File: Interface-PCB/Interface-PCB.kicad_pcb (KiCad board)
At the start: 2 copper layers, 100 x 100 mm, 0 parts

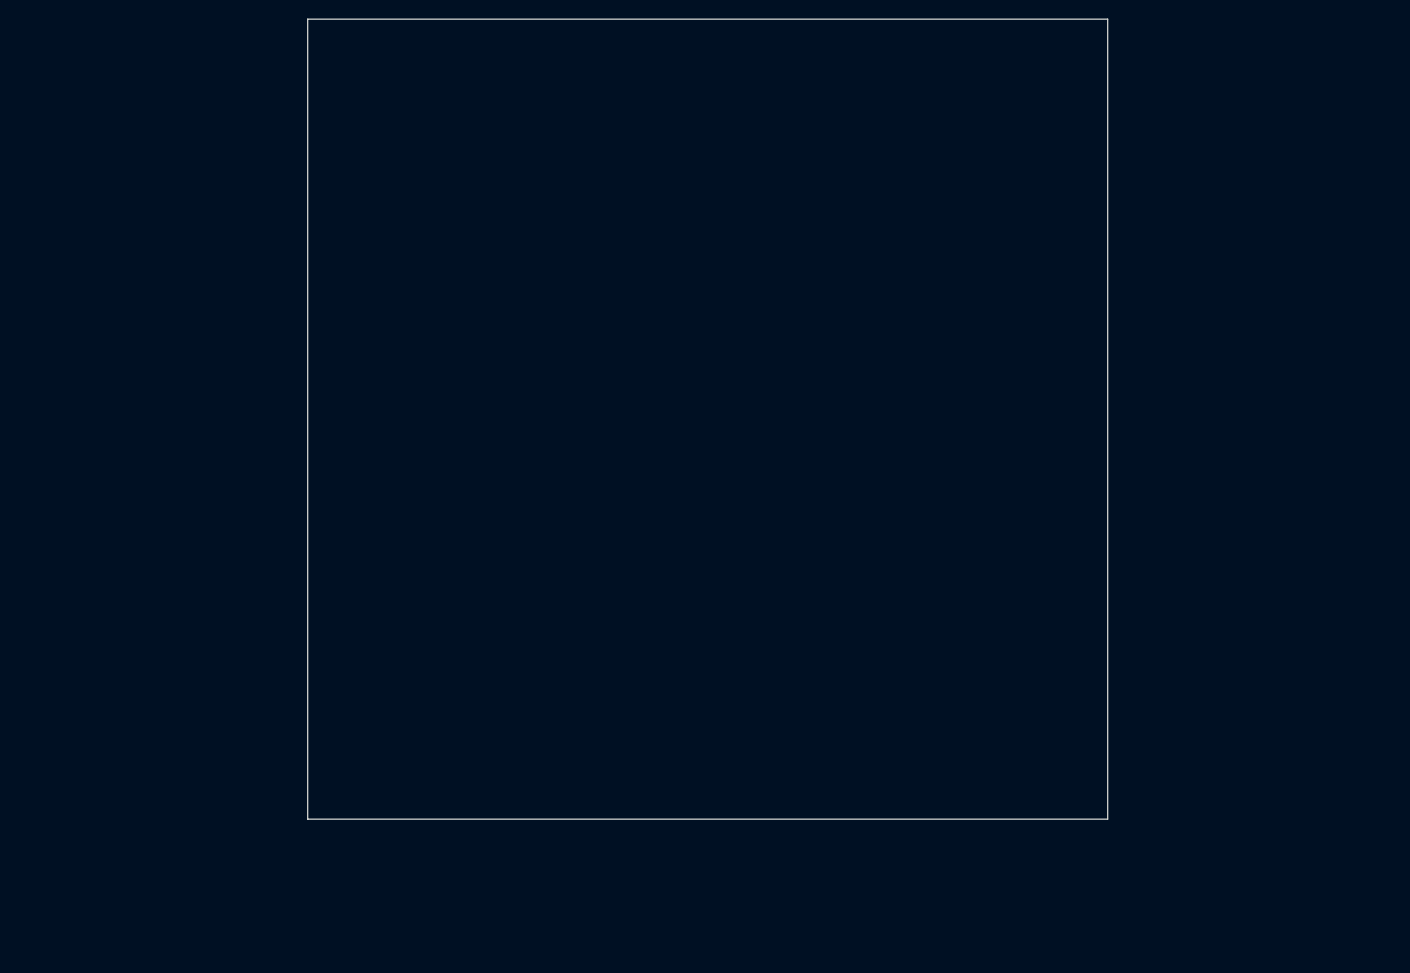
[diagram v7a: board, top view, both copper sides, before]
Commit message: Complete Initial Layout of PCB
- aligned to 5mm grid
- 100x100mm board
- update footprints
- align 2 resistors to 2.54mm spacing
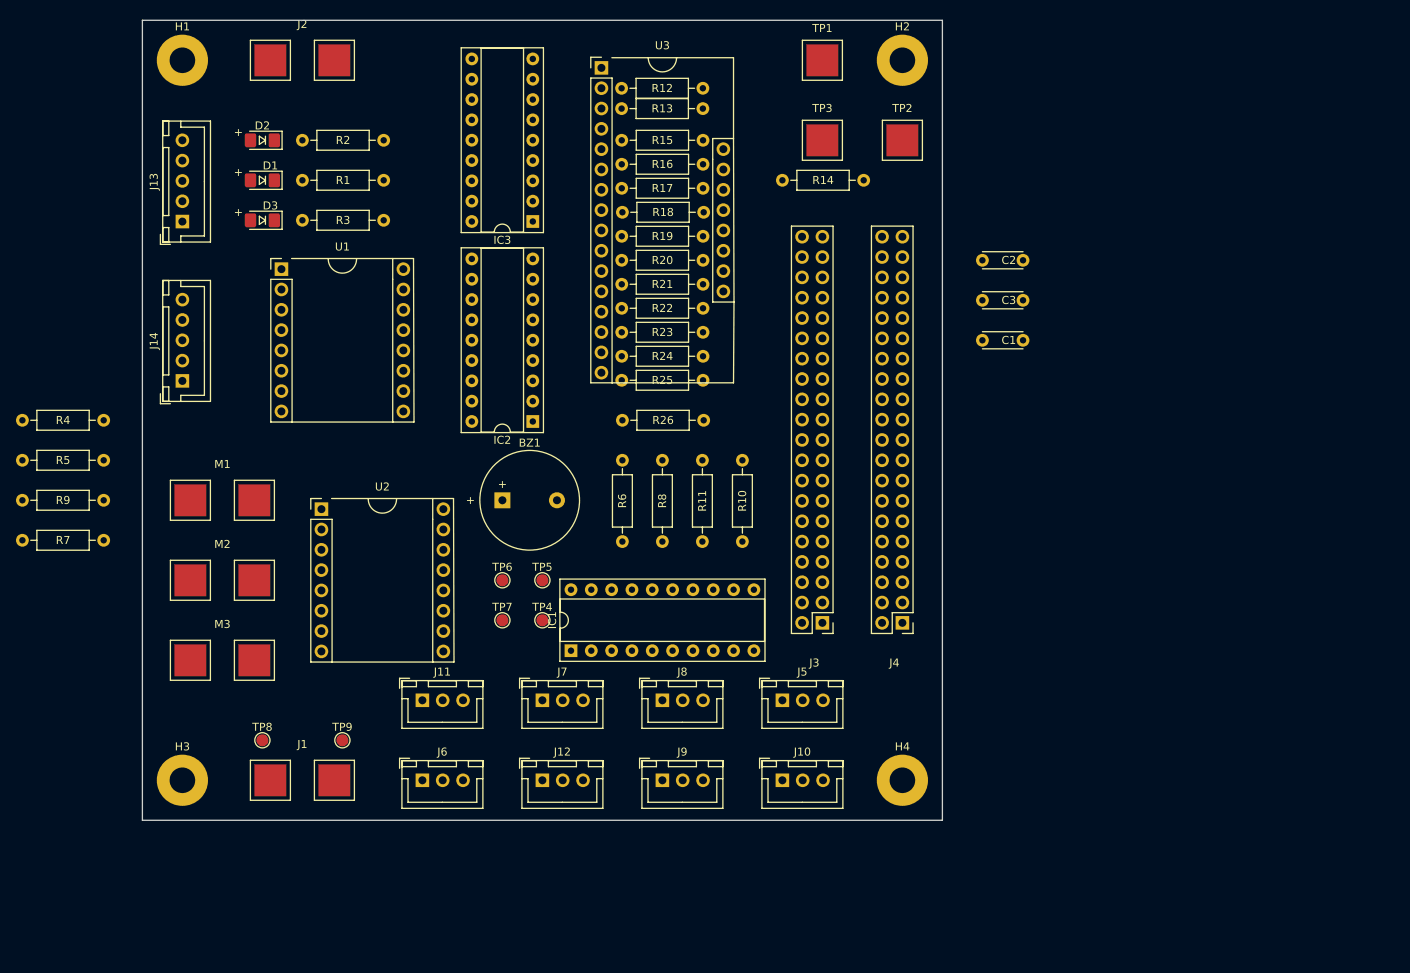
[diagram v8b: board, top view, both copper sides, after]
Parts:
- added BZ1: Buzzer, AA_Custom_Components:Buzzer_Generic_D12.2mm_H6.5mm, F.Cu at (125.0, 110.0)
- added C1: 100nF, AA_Custom_Components:C_Ceramic_Disc_D4.3mm_W1.9mm_P5.08mm, F.Cu at (185.0, 90.0)
- added C2: 100nF, AA_Custom_Components:C_Ceramic_Disc_D4.3mm_W1.9mm_P5.08mm, F.Cu at (185.0, 80.0)
- added C3: 100nF, AA_Custom_Components:C_Ceramic_Disc_D4.3mm_W1.9mm_P5.08mm, F.Cu at (185.0, 85.0)
- added D1: 12V_ON, AA_Custom_Components:LED_SS_1206_3216Metric_Pad1.42x1.75mm_HandSolder, F.Cu at (95.0, 70.0)
- added D2: USER_LED, AA_Custom_Components:LED_SS_1206_3216Metric_Pad1.42x1.75mm_HandSolder, F.Cu at (95.0, 65.0)
- added D3: 5V_ON, AA_Custom_Components:LED_SS_1206_3216Metric_Pad1.42x1.75mm_HandSolder, F.Cu at (95.0, 75.0)
- added H1: MountingHole, MountingHole:MountingHole_3.2mm_M3_Pad, F.Cu at (85.0, 55.0)
- added H2: MountingHole, MountingHole:MountingHole_3.2mm_M3_Pad, F.Cu at (175.0, 55.0)
- added H3: MountingHole, MountingHole:MountingHole_3.2mm_M3_Pad, F.Cu at (85.0, 145.0)
- added H4: MountingHole, MountingHole:MountingHole_3.2mm_M3_Pad, F.Cu at (175.0, 145.0)
- added IC1: SN74LVC245AN, AA_Custom_Components:DIP-20_W7.62mm_Socket_IC, F.Cu at (133.6, 128.8)
- added IC2: TBD62783APG, AA_Custom_Components:DIP-18_W7.62mm_Socket_IC, F.Cu at (128.8, 100.2)
- added IC3: TBD62783APG, AA_Custom_Components:DIP-18_W7.62mm_Socket_IC, F.Cu at (128.8, 75.2)
- added J1: BARREL_JACK_PAD, AA_Custom_Components:PowerPad_Pair_4.0x4.0mm, F.Cu at (100.0, 145.0)
- added J10: LEVEL_SENSOR, AA_Custom_Components:JST_XH_1x03_P2.54mm_Vertical, F.Cu at (160.0, 145.0)
- added J11: TEMPERATURE_SENSOR, AA_Custom_Components:JST_XH_1x03_P2.54mm_Vertical, F.Cu at (115.0, 135.0)
- added J12: TEMPERATURE_SENSOR, AA_Custom_Components:JST_XH_1x03_P2.54mm_Vertical, F.Cu at (130.0, 145.0)
- added J13: CONN_05JST, AA_Custom_Components:JST_XH_1x05_P2.54mm_Vertical, F.Cu at (85.0, 75.2)
- added J14: CONN_05JST, AA_Custom_Components:JST_XH_1x05_P2.54mm_Vertical, F.Cu at (85.0, 95.1)
- added J2: BARREL_JACK_PAD, AA_Custom_Components:PowerPad_Pair_4.0x4.0mm, F.Cu at (100.0, 55.0)
- added J3: GPIO_DEBUG_HEADER, AA_Custom_Components:RASPBERRYPI-40-PIN-GPIO-2x20_P2.54mm_Vertical, F.Cu at (165.0, 125.3)
- added J4: RASPBERRYPI_GPIO_CONN_HEADER, AA_Custom_Components:RASPBERRYPI-40-PIN-GPIO-2x20_P2.54mm_Vertical, F.Cu at (175.0, 125.3)
- added J5: LEVEL_SENSOR, AA_Custom_Components:JST_XH_1x03_P2.54mm_Vertical, F.Cu at (160.0, 135.0)
- added J6: LEVEL_SENSOR, AA_Custom_Components:JST_XH_1x03_P2.54mm_Vertical, F.Cu at (115.0, 145.0)
- added J7: LEVEL_SENSOR, AA_Custom_Components:JST_XH_1x03_P2.54mm_Vertical, F.Cu at (130.0, 135.0)
- added J8: LEVEL_SENSOR, AA_Custom_Components:JST_XH_1x03_P2.54mm_Vertical, F.Cu at (145.0, 135.0)
- added J9: LEVEL_SENSOR, AA_Custom_Components:JST_XH_1x03_P2.54mm_Vertical, F.Cu at (145.0, 145.0)
- added M1: PERISTALTIC_PUMP, AA_Custom_Components:PowerPad_Pair_4.0x4.0mm, F.Cu at (90.0, 110.0)
- added M2: PERISTALTIC_PUMP, AA_Custom_Components:PowerPad_Pair_4.0x4.0mm, F.Cu at (90.0, 120.0)
- added M3: PERISTALTIC_PUMP, AA_Custom_Components:PowerPad_Pair_4.0x4.0mm, F.Cu at (90.0, 130.0)
- added R1: 680, AA_Custom_Components:R_SS_Axial_DIN0207_L6.3mm_D2.5mm_P10.16mm_Horizontal, F.Cu at (100.0, 70.0)
- added R10: 10k, AA_Custom_Components:R_SS_Axial_DIN0207_L6.3mm_D2.5mm_P10.16mm_Horizontal, F.Cu at (155.0, 105.0)
- added R11: 10k, AA_Custom_Components:R_SS_Axial_DIN0207_L6.3mm_D2.5mm_P10.16mm_Horizontal, F.Cu at (150.0, 105.0)
- added R12: 10k, AA_Custom_Components:R_SS_Axial_DIN0207_L6.3mm_D2.5mm_P10.16mm_Horizontal, F.Cu at (139.9, 58.5)
- added R13: 10k, AA_Custom_Components:R_SS_Axial_DIN0207_L6.3mm_D2.5mm_P10.16mm_Horizontal, F.Cu at (139.9, 61.0)
- added R14: 10k, AA_Custom_Components:R_SS_Axial_DIN0207_L6.3mm_D2.5mm_P10.16mm_Horizontal, F.Cu at (160.0, 70.0)
- added R15: 10k, AA_Custom_Components:R_SS_Axial_DIN0207_L6.3mm_D2.5mm_P10.16mm_Horizontal, F.Cu at (139.9, 65.0)
- added R16: 10k, AA_Custom_Components:R_SS_Axial_DIN0207_L6.3mm_D2.5mm_P10.16mm_Horizontal, F.Cu at (139.9, 68.0)
- added R17: 10k, AA_Custom_Components:R_SS_Axial_DIN0207_L6.3mm_D2.5mm_P10.16mm_Horizontal, F.Cu at (139.9, 71.0)
- added R18: 10k, AA_Custom_Components:R_SS_Axial_DIN0207_L6.3mm_D2.5mm_P10.16mm_Horizontal, F.Cu at (140.0, 74.0)
- added R19: 10k, AA_Custom_Components:R_SS_Axial_DIN0207_L6.3mm_D2.5mm_P10.16mm_Horizontal, F.Cu at (139.9, 77.0)
- added R2: 100, AA_Custom_Components:R_SS_Axial_DIN0207_L6.3mm_D2.5mm_P10.16mm_Horizontal, F.Cu at (100.0, 65.0)
- added R20: 10k, AA_Custom_Components:R_SS_Axial_DIN0207_L6.3mm_D2.5mm_P10.16mm_Horizontal, F.Cu at (139.9, 80.0)
- added R21: 10k, AA_Custom_Components:R_SS_Axial_DIN0207_L6.3mm_D2.5mm_P10.16mm_Horizontal, F.Cu at (139.9, 83.0)
- added R22: 10k, AA_Custom_Components:R_SS_Axial_DIN0207_L6.3mm_D2.5mm_P10.16mm_Horizontal, F.Cu at (139.9, 86.0)
- added R23: 10k, AA_Custom_Components:R_SS_Axial_DIN0207_L6.3mm_D2.5mm_P10.16mm_Horizontal, F.Cu at (139.9, 89.0)
- added R24: 10k, AA_Custom_Components:R_SS_Axial_DIN0207_L6.3mm_D2.5mm_P10.16mm_Horizontal, F.Cu at (139.9, 92.0)
- added R25: 10k, AA_Custom_Components:R_SS_Axial_DIN0207_L6.3mm_D2.5mm_P10.16mm_Horizontal, F.Cu at (139.9, 95.0)
- added R26: 10k, AA_Custom_Components:R_SS_Axial_DIN0207_L6.3mm_D2.5mm_P10.16mm_Horizontal, F.Cu at (140.0, 100.0)
- added R3: 220, AA_Custom_Components:R_SS_Axial_DIN0207_L6.3mm_D2.5mm_P10.16mm_Horizontal, F.Cu at (100.0, 75.0)
- added R4: 220, AA_Custom_Components:R_SS_Axial_DIN0207_L6.3mm_D2.5mm_P10.16mm_Horizontal, F.Cu at (65.0, 100.0)
- added R5: 220, AA_Custom_Components:R_SS_Axial_DIN0207_L6.3mm_D2.5mm_P10.16mm_Horizontal, F.Cu at (65.0, 105.0)
- added R6: 220, AA_Custom_Components:R_SS_Axial_DIN0207_L6.3mm_D2.5mm_P10.16mm_Horizontal, F.Cu at (140.0, 105.0)
- added R7: 220, AA_Custom_Components:R_SS_Axial_DIN0207_L6.3mm_D2.5mm_P10.16mm_Horizontal, F.Cu at (65.0, 115.0)
- added R8: 220, AA_Custom_Components:R_SS_Axial_DIN0207_L6.3mm_D2.5mm_P10.16mm_Horizontal, F.Cu at (145.0, 105.0)
- added R9: 220, AA_Custom_Components:R_SS_Axial_DIN0207_L6.3mm_D2.5mm_P10.16mm_Horizontal, F.Cu at (65.0, 110.0)
- added TP1: GND_PAD, AA_Custom_Components:TestPoint_Pad_4.0x4.0mm, F.Cu at (165.0, 55.0)
- added TP2: 5V_PAD, AA_Custom_Components:TestPoint_Pad_4.0x4.0mm, F.Cu at (175.0, 65.0)
- added TP3: 3.3V_PAD, AA_Custom_Components:TestPoint_Pad_4.0x4.0mm, F.Cu at (165.0, 65.0)
- added TP4: PAD, TestPoint:TestPoint_Pad_D1.5mm, F.Cu at (130.0, 125.0)
- added TP5: PAD, TestPoint:TestPoint_Pad_D1.5mm, F.Cu at (130.0, 120.0)
- added TP6: PAD, TestPoint:TestPoint_Pad_D1.5mm, F.Cu at (125.0, 120.0)
- added TP7: PAD, TestPoint:TestPoint_Pad_D1.5mm, F.Cu at (125.0, 125.0)
- added TP8: PAD, TestPoint:TestPoint_Pad_D1.5mm, F.Cu at (95.0, 140.0)
- added TP9: PAD, TestPoint:TestPoint_Pad_D1.5mm, F.Cu at (105.0, 140.0)
- added U1: TB6612FNG_BREAKOUT, AA_Custom_Components:TB6612FNG_Breakout, F.Cu at (105.0, 90.0)
- added U2: TB6612FNG_BREAKOUT, AA_Custom_Components:TB6612FNG_Breakout, F.Cu at (110.0, 120.0)
- added U3: CD74HC4067_MUX_BREAKOUT, AA_Custom_Components:CD74HC4067_MUX_BREAKOUT, F.Cu at (145.0, 75.0)
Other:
- board text removed: "0.1270 mm / 0.1270 mm"
- board text removed: "0.2000 mm"
- board text removed: "1.6000 mm"
- board text removed: "100.0500 mm x 100.0500 mm"
- board text removed: "2"
- board text removed: "BOARD CHARACTERISTICS"
- board text removed: "Board Thickness:"
- board text removed: "Board overall dimensions:"
- board text removed: "Castellated pads:"
- board text removed: "Copper Finish:"
- board text removed: "Copper Layer Count:"
- board text removed: "Edge card connectors:"
- board text removed: "HAL SnPb"
- board text removed: "Impedance Control:"
- board text removed: "Min hole diameter:"
- board text removed: "Min track/spacing:"
- board text removed: "No"
- board text removed: "Plated Board Edge:"
